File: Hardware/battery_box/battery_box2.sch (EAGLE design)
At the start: 49 parts, among them IC1 AD826R, IC2 LM2574, IC3 PIC16F1824, IC4 LD117AS18TR, J1 CON_HEADER_PRG_PIC_ICSPA, Q1 IRFR5505PBFTO252, Q2 BSS123, X1 CON_MOLEX_39_29_1028, X2 KUSBVX

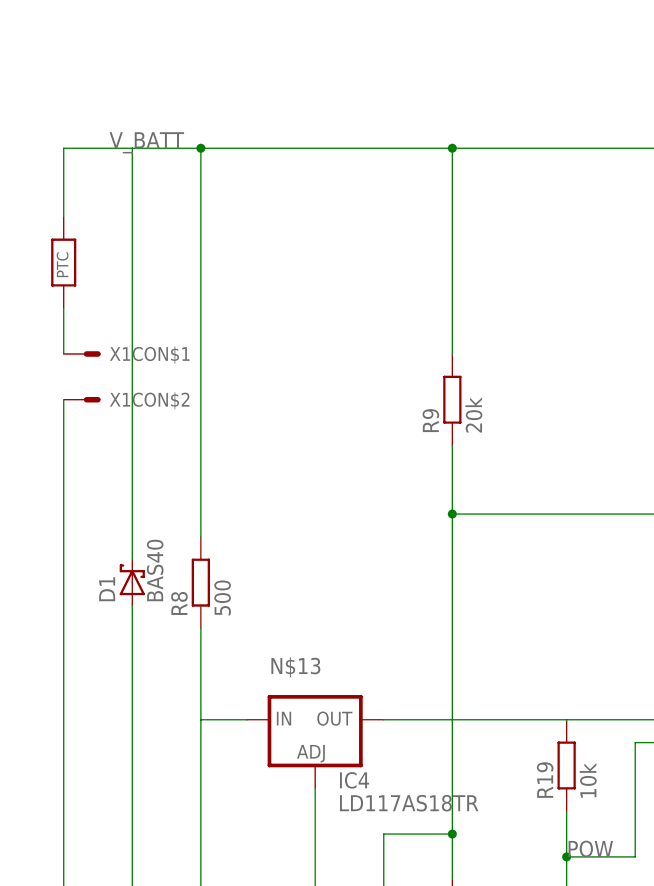
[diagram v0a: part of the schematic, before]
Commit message: Cleaned up and routed PCB and Schematic files
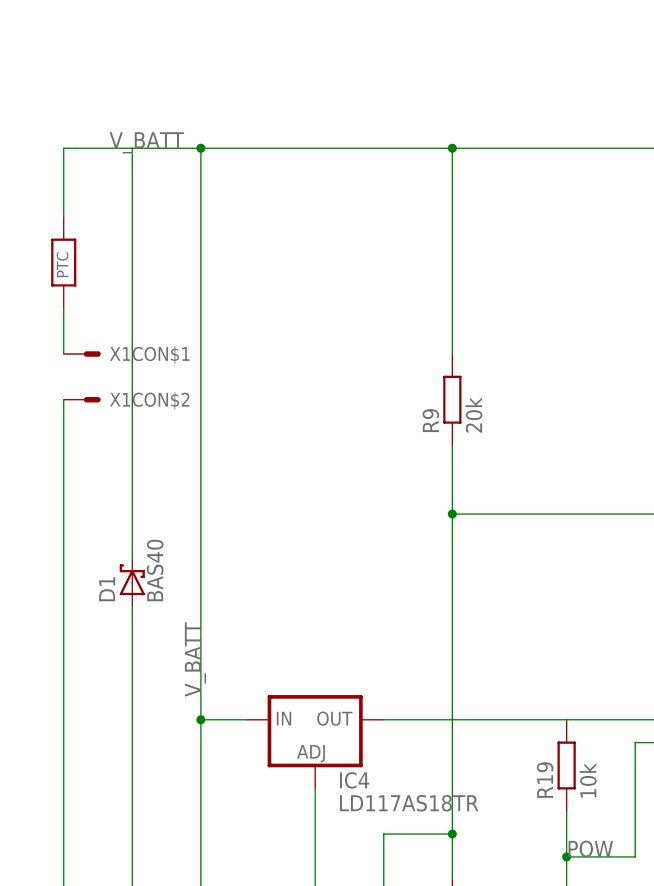
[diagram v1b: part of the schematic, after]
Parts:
- removed R8: 500, rcl:R-EU_R0805
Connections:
- net N$1 renamed 12V_OUT
- net N$20 renamed GND_OUTPUT
- removed net N$13: C5.1, IC4.IN, R8.1
- net V_BATT: now also C5.1, IC4.IN; no longer R8.2
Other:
- note removed: "Add Reverse Battery Protection Diode:"
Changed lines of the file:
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@@
 <?xml version="1.0" encoding="utf-8"?>
 <!DOCTYPE eagle SYSTEM "eagle.dtd">
-<eagle version="6.4">
+<eagle version="6.3">
 <drawing>
 <settings>
@@
 <part name="SW_POW" library="SparkFun" deviceset="TAC_SWITCH" device="PTH"/>
 <part name="U$2" library="equinox" deviceset="PTC" device=""/>
-<part name="R8" library="rcl" deviceset="R-EU_" device="R0805" value="500"/>
 <part name="IC3" library="equinox" deviceset="PIC16F1824" device=""/>
 <part name="R9" library="rcl" deviceset="R-EU_" device="R0805" value="20k"/>
@@
 <text x="190.5" y="7.62" size="1.778" layer="98">PCB Mounts</text>
 <text x="353.06" y="111.76" size="1.778" layer="98" rot="R90">Farnell: 1865265</text>
-<text x="45.72" y="142.24" size="1.778" layer="98" rot="R90">Add Reverse Battery Protection Diode:</text>
 </plain>
 <instances>
@@
 <instance part="SW_POW" gate="S" x="81.28" y="86.36" rot="R270"/>
 <instance part="U$2" gate="G$1" x="25.4" y="167.64" rot="R90"/>
-<instance part="R8" gate="G$1" x="40.64" y="134.62" rot="R90"/>
 <instance part="IC3" gate="G$1" x="106.68" y="124.46"/>
 <instance part="R9" gate="G$1" x="68.58" y="154.94" rot="R90"/>
@@
 <net name="V_BATT" class="1">
 <segment>
-<wire x1="40.64" y1="182.88" x2="40.64" y2="139.7" width="0.1524" layer="91"/>
+<wire x1="40.64" y1="182.88" x2="40.64" y2="119.38" width="0.1524" layer="91"/>
 <label x="30.48" y="182.88" size="1.778" layer="95"/>
 <wire x1="25.4" y1="182.88" x2="33.02" y2="182.88" width="0.1524" layer="91"/>
@@
 <wire x1="68.58" y1="182.88" x2="40.64" y2="182.88" width="0.1524" layer="91"/>
 <wire x1="25.4" y1="175.26" x2="25.4" y2="182.88" width="0.1524" layer="91"/>
-<pinref part="R8" gate="G$1" pin="2"/>
 <pinref part="R9" gate="G$1" pin="2"/>
 <wire x1="68.58" y1="160.02" x2="68.58" y2="182.88" width="0.1524" layer="91"/>
@@
 <wire x1="170.18" y1="193.04" x2="160.02" y2="193.04" width="0.1524" layer="91"/>
 <wire x1="160.02" y1="193.04" x2="160.02" y2="182.88" width="0.1524" layer="91"/>
+<label x="40.64" y="121.92" size="1.778" layer="95" rot="R90"/>
+<pinref part="IC4" gate="G$1" pin="IN"/>
+<wire x1="45.72" y1="119.38" x2="40.64" y2="119.38" width="0.1524" layer="91"/>
+<wire x1="40.64" y1="119.38" x2="40.64" y2="99.06" width="0.1524" layer="91"/>
+<pinref part="C5" gate="G$1" pin="1"/>
+<junction x="40.64" y="119.38"/>
 </segment>
 </net>
@@
 </segment>
 </net>
-<net name="N$1" class="1">
+<net name="12V_OUT" class="1">
 <segment>
 <pinref part="Q1" gate="G$1" pin="D"/>
@@
 </segment>
 </net>
-<net name="N$20" class="1">
+<net name="GND_OUTPUT" class="1">
 <segment>
 <pinref part="X2" gate="G$1" pin="S2"/>
@@
 </segment>
 </net>
-<net name="N$13" class="0">
-<segment>
-<pinref part="R8" gate="G$1" pin="1"/>
-<wire x1="40.64" y1="129.54" x2="40.64" y2="119.38" width="0.1524" layer="91"/>
-<label x="48.26" y="124.46" size="1.778" layer="95"/>
-<pinref part="IC4" gate="G$1" pin="IN"/>
-<wire x1="45.72" y1="119.38" x2="40.64" y2="119.38" width="0.1524" layer="91"/>
-<wire x1="40.64" y1="119.38" x2="40.64" y2="99.06" width="0.1524" layer="91"/>
-<pinref part="C5" gate="G$1" pin="1"/>
-</segment>
-</net>

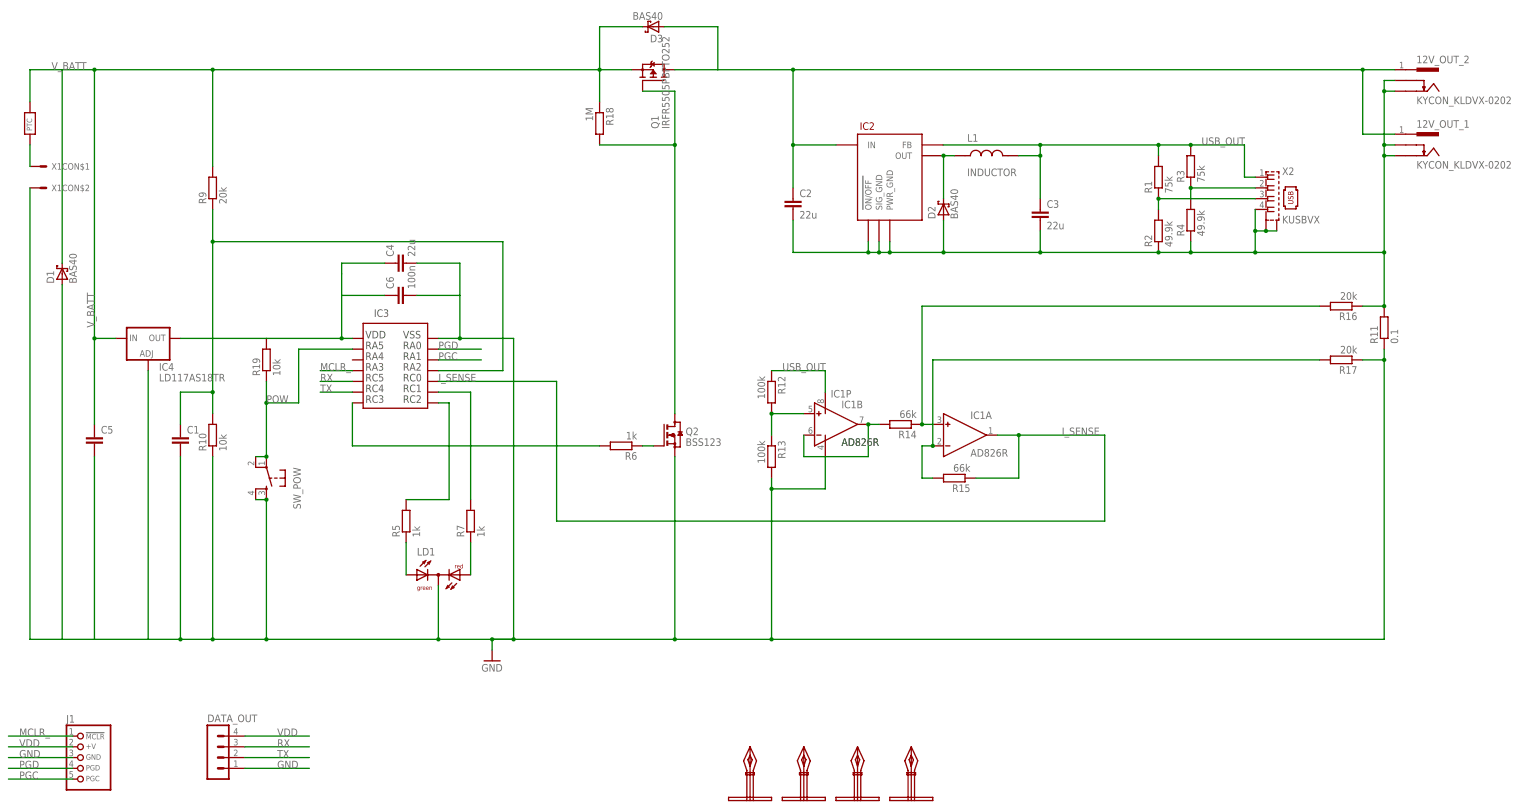
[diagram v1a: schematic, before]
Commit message: Added new components with correct footprints
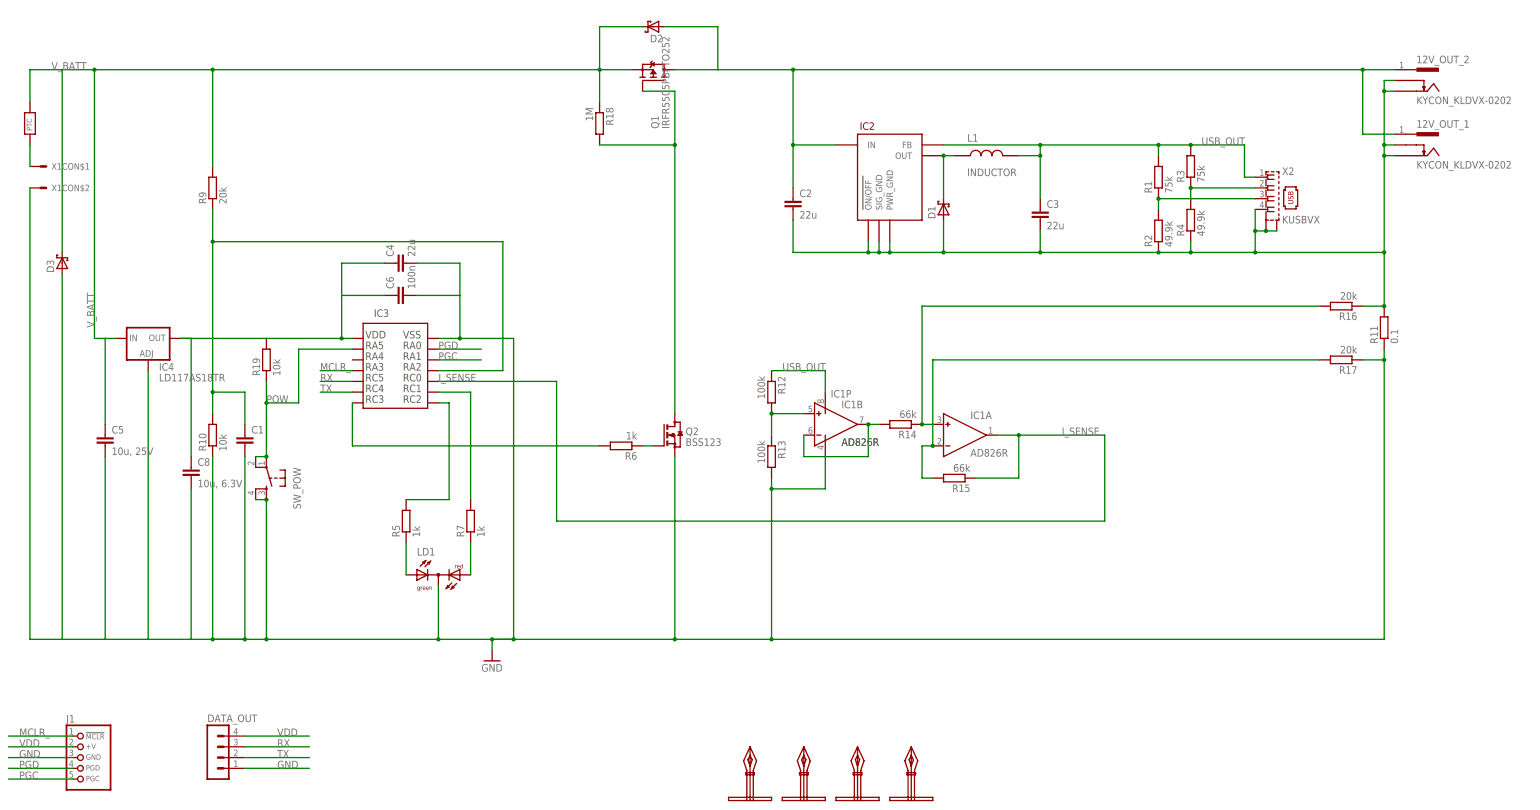
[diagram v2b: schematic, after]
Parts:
- added C8: 10u, 6.3V, rcl:C-EUC0805
- C5: value (none) -> 10u, 25V; device rcl:C-EUC0805 -> rcl:C-EUC1210
- C6: device rcl:C-EUC0805 -> rcl:C-EUC0402
- D1: value BAS40 -> (none); device diode:BAS40 -> diode:SCHOTTKY-DIODESMD
- D2, D3: value BAS40 -> (none); device diode:BAS40 -> diode:SCHOTTKY-DIODESMC
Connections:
- net 12V_OUT: now also D2.A; no longer D3.A
- net GND: now also C8.2, D3.A; no longer D1.A
- net GND_OUTPUT: now also D1.A; no longer D2.A
- net N$9: now also D1.C; no longer D2.C
- net VDD: now also C8.1
- net V_BATT: now also D2.C; no longer D1.C
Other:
- moved on the sheet: C1, C5

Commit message: Re-routed PCB
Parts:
- C6: device rcl:C-EUC0402 -> resistor:C-EUC0805
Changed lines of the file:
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@@
 <?xml version="1.0" encoding="utf-8"?>
 <!DOCTYPE eagle SYSTEM "eagle.dtd">
-<eagle version="6.4">
+<eagle version="6.3">
 <drawing>
 <settings>
@@
 <part name="C5" library="rcl" deviceset="C-EU" device="C1210" value="10u, 25V"/>
 <part name="D1" library="diode" deviceset="SCHOTTKY-DIODE" device="SMD"/>
-<part name="C6" library="rcl" deviceset="C-EU" device="C0402" value="100n"/>
+<part name="C6" library="resistor" deviceset="C-EU" device="C0805" value="100n"/>
 </parts>
 <sheets>
